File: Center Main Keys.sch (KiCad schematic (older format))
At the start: 9 parts

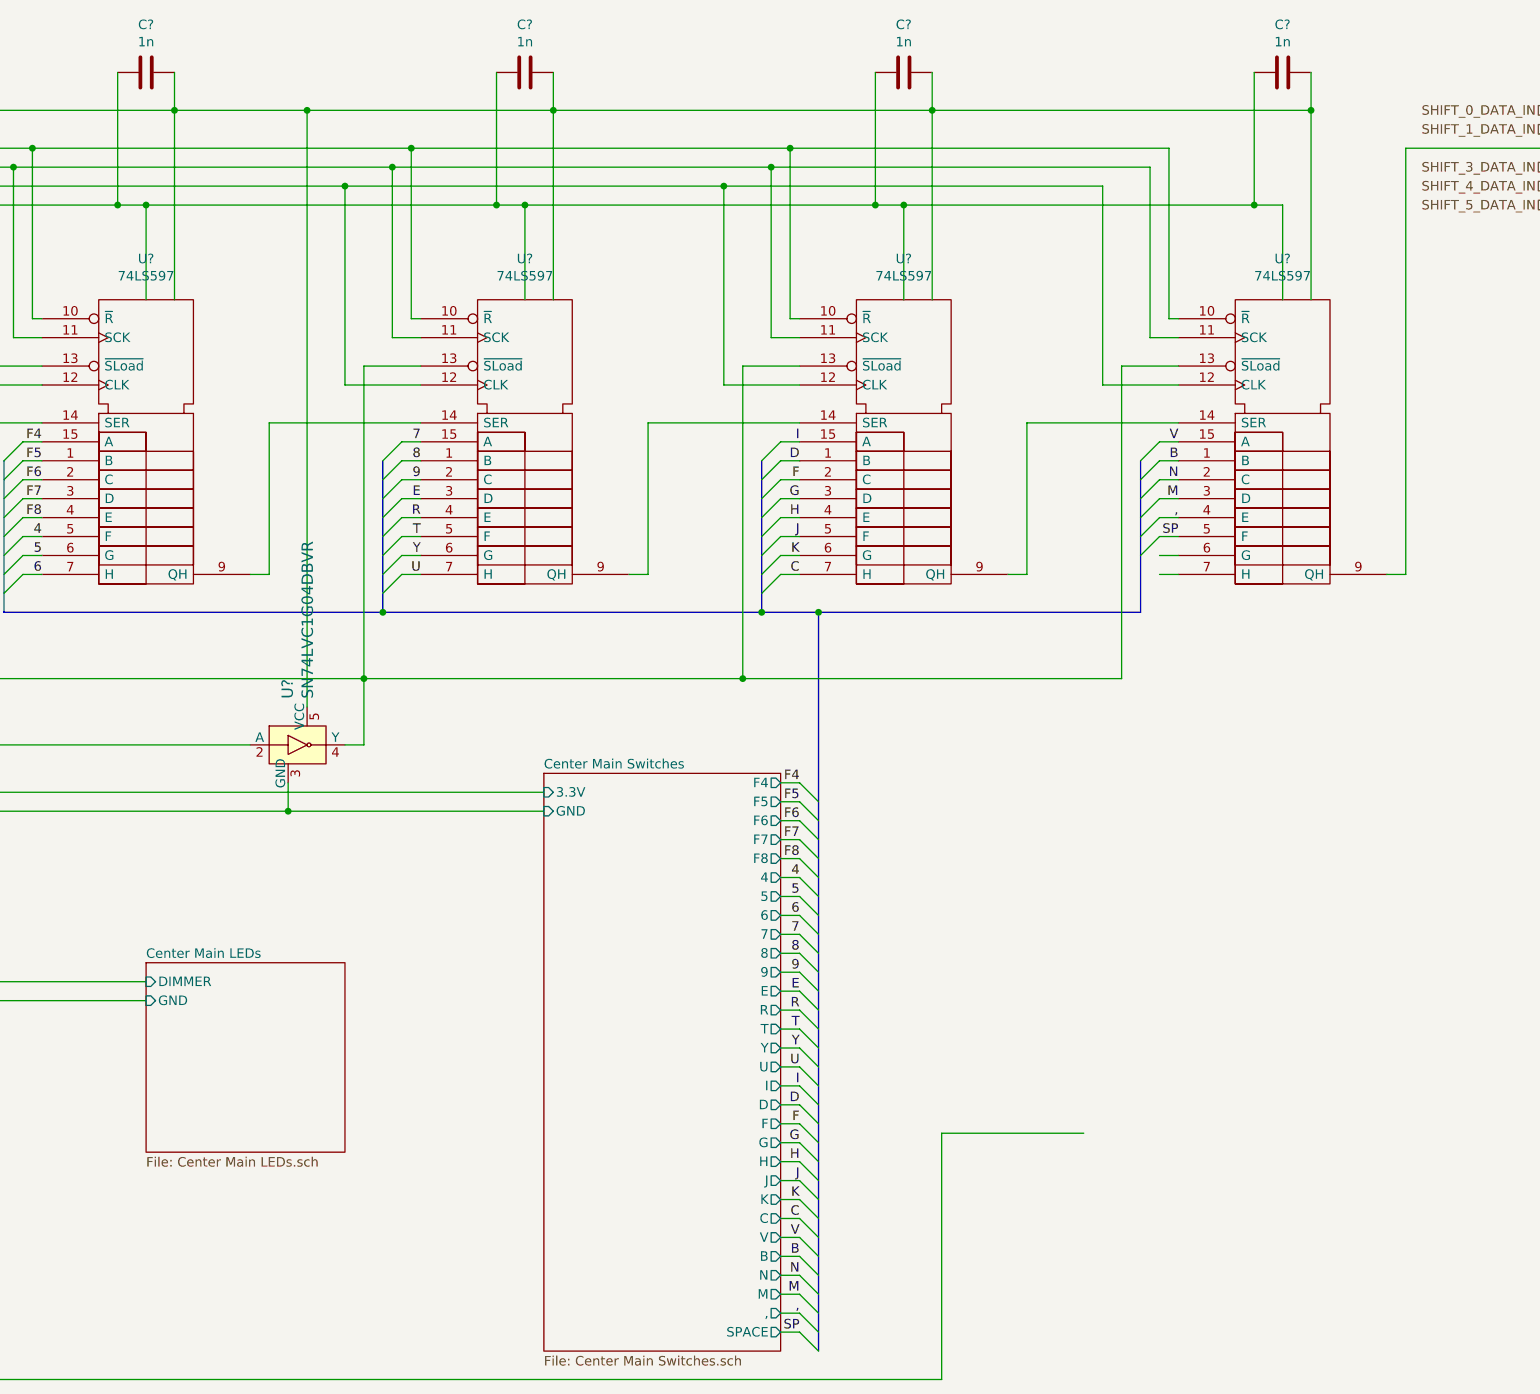
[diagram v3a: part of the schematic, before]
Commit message: Corrected errors found in design rule check
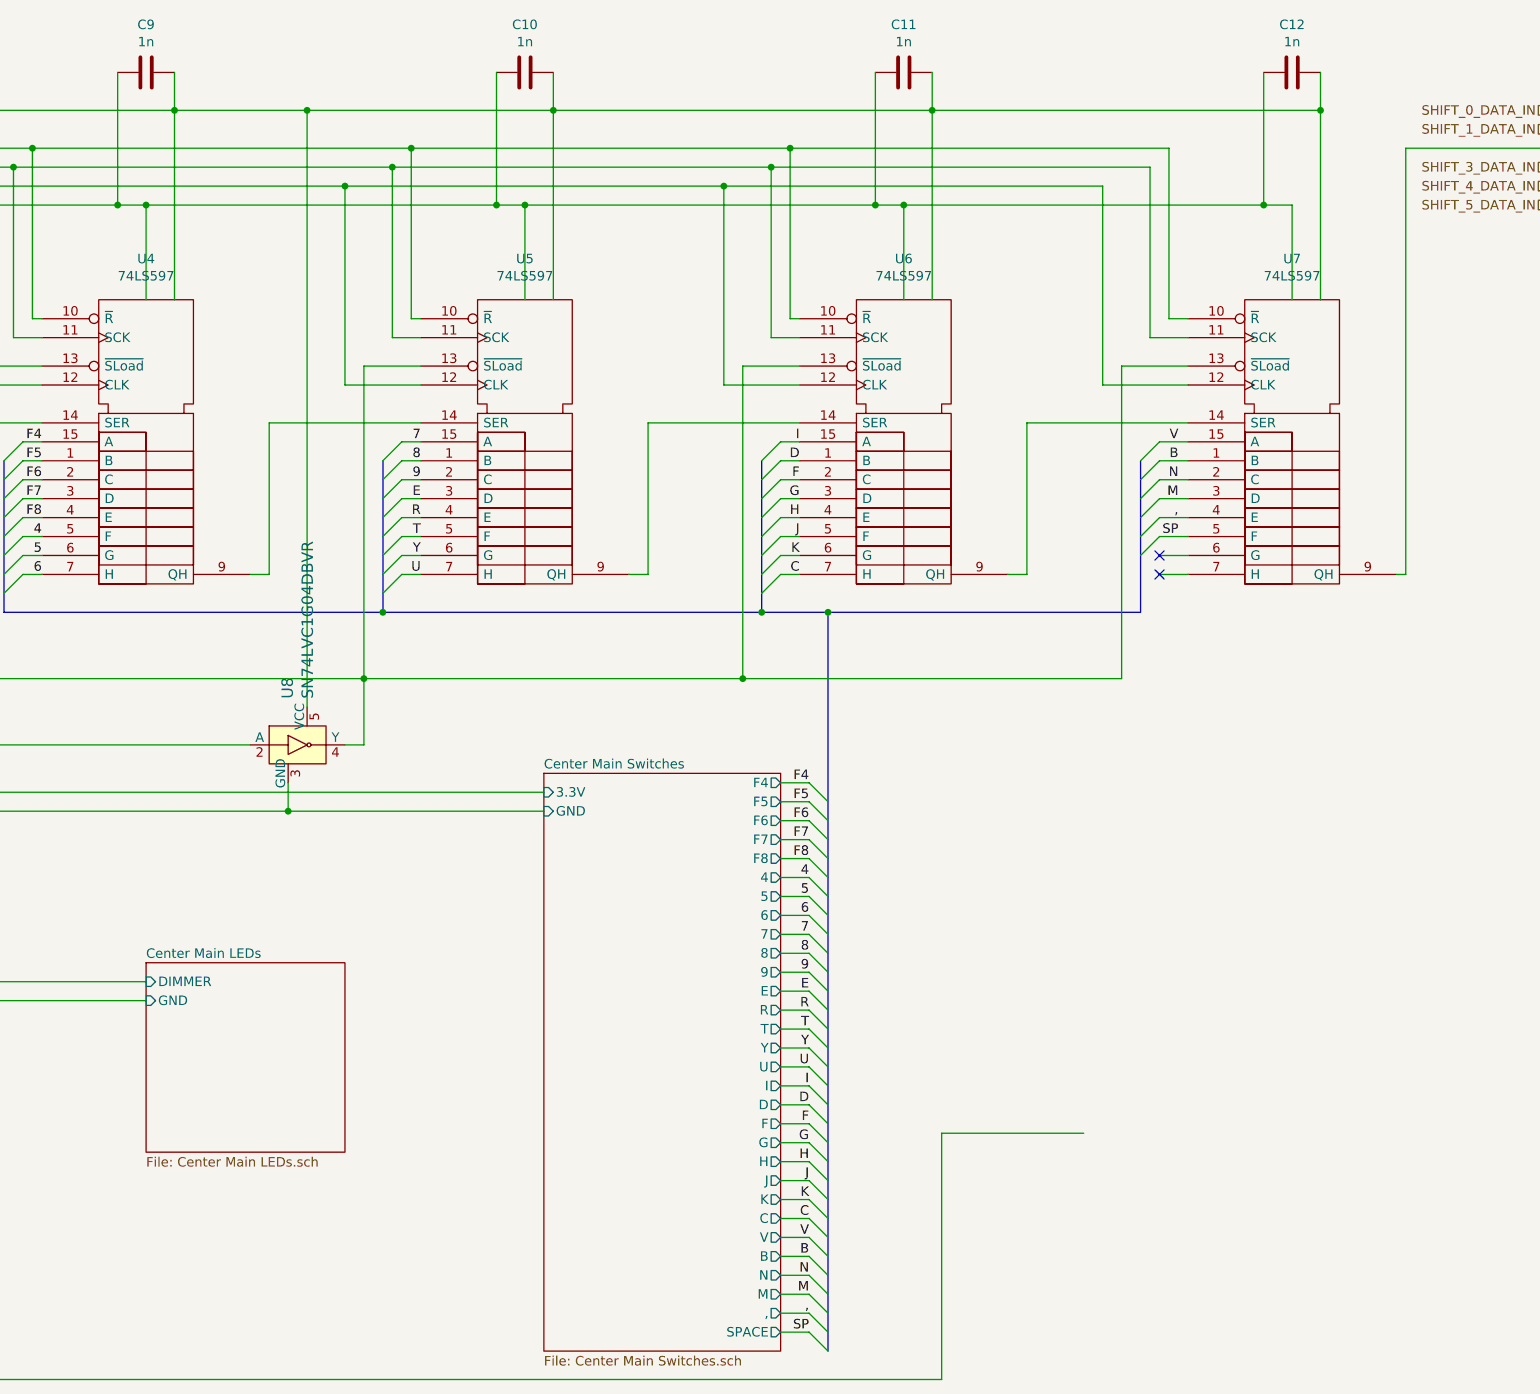
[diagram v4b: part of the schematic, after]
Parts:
- C10, C11, C12, C9: renamed from C?; footprint (none) -> Capacitor_SMD:C_1206_3216Metric_Pad1.42x1.75mm_HandSolder
- U4, U5, U6, U7: renamed from U?; footprint (none) -> Package_SO:SOIC-16_3.9x9.9mm_P1.27mm
- gave numbers to parts that had none: 1
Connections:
- no-connect marks 0 -> 2
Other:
- moved on the sheet: C12, U7

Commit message: Redesigned for single large PCB
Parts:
- added C13, C14, C15, C16, C17, C18, C19, C20, C21, C22: 1n, Capacitor_SMD:C_1206_3216Metric_Pad1.42x1.75mm_HandSolder, symbol Device:C
- added U10, U11, U12, U13, U14, U15, U16, U17, U18, U9: 74LS597, Package_SO:SOIC-16_3.9x9.9mm_P1.27mm, symbol 74xx_IEEE:74LS597
- renumbered U8 to U4, U4 to U5, U5 to U6, U6 to U7, U7 to U8
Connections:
- net ,: now also U13.5 (F); no longer U8.4 (E)
- net 4: now also U10.6 (G); no longer U5.5 (F)
- net 5: now also U10.7 (H); no longer U5.6 (G)
- net 6: now also U11.15 (A); no longer U5.7 (H)
- net 7: now also U11.1 (B); no longer U6.15 (A)
- net 8: now also U11.2 (C); no longer U6.1 (B)
- net 9: now also U11.3 (D); no longer U6.2 (C)
- net B: now also U13.2 (C); no longer U8.1 (B)
- net C: now also U13.15 (A); no longer U7.7 (H)
- net D: now also U12.2 (C); no longer U7.1 (B)
- net E: now also U11.4 (E); no longer U6.3 (D)
- net F: now also U12.3 (D); no longer U7.2 (C)
- net F4: now also U10.1 (B); no longer U5.15 (A)
- net F5: now also U10.2 (C); no longer U5.1 (B)
- net F6: now also U10.3 (D); no longer U5.2 (C)
- net F7: now also U10.4 (E); no longer U5.3 (D)
- net F8: now also U10.5 (F); no longer U5.4 (E)
- net G: now also U12.4 (E); no longer U7.3 (D)
- net GND: now also C13.2, C14.2, C15.2, C16.2, C17.2, C18.2, C19.2, C20.2, C21.2, C22.2, U10.8 (GND), U11.8 (GND), U12.8 (GND), U13.8 (GND), U14.8 (GND), U15.8 (GND), U16.8 (GND), U17.8 (GND), U18.8 (GND), U9.8 (GND)
- net H: now also U12.5 (F); no longer U7.4 (E)
- net I: now also U12.1 (B); no longer U7.15 (A)
- net J: now also U12.6 (G); no longer U7.5 (F)
- net K: now also U12.7 (H); no longer U7.6 (G)
- net M: now also U13.4 (E); no longer U8.3 (D)
- net N: now also U13.3 (D); no longer U8.2 (C)
- net R: now also U11.5 (F); no longer U6.4 (E)
- net RESET: now also U10.10 (~R), U11.10 (~R), U12.10 (~R), U13.10 (~R), U14.10 (~R), U15.10 (~R), U16.10 (~R), U17.10 (~R), U18.10 (~R), U9.10 (~R)
- net SHIFT_CLK: now also U10.11 (SCK), U11.11 (SCK), U12.11 (SCK), U13.11 (SCK), U14.11 (SCK), U15.11 (SCK), U16.11 (SCK), U17.11 (SCK), U18.11 (SCK), U9.11 (SCK)
- net SHIFT_RCLK: now also U10.12 (CLK), U11.12 (CLK), U12.12 (CLK), U13.12 (CLK), U14.12 (CLK), U15.12 (CLK), U16.12 (CLK), U17.12 (CLK), U18.12 (CLK), U9.12 (CLK)
- net SP: now also U13.6 (G); no longer U8.5 (F)
- net T: now also U11.6 (G); no longer U6.5 (F)
- net U: now also U12.15 (A); no longer U6.7 (H)
- net V: now also U13.1 (B); no longer U8.15 (A)
- net VCC: now also C13.1, C14.1, C15.1, C16.1, C17.1, C18.1, C19.1, C20.1, C21.1, C22.1, U10.16 (VCC), U11.16 (VCC), U12.16 (VCC), U13.16 (VCC), U14.16 (VCC), U15.16 (VCC), U16.16 (VCC), U17.16 (VCC), U18.16 (VCC), U9.16 (VCC)
- net Y: now also U11.7 (H); no longer U6.6 (G)
- net at U4.4 (Y), U5.13 (~SLoad), U6.13 (~SLoad)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: now also U10.13 (~SLoad), U11.13 (~SLoad), U12.13 (~SLoad), U13.13 (~SLoad), U14.13 (~SLoad), U15.13 (~SLoad), U16.13 (~SLoad), U17.13 (~SLoad), U18.13 (~SLoad), U9.13 (~SLoad)
- net Q: now reaches U8.6 (G)
- net W: now reaches U8.7 (H)
- net SHIFT_2_DATA: no longer names the net of U8.9 (QH)
- net SHIFT_2_DATA: now also U9.14 (SER)
- new net: U10.14 (SER), U9.9 (QH)
- new net: U10.9 (QH), U11.14 (SER)
- new net: U11.9 (QH), U12.14 (SER)
- new net: U12.9 (QH), U13.14 (SER)
- new net: U13.9 (QH), U14.14 (SER)
- new net: U14.9 (QH), U15.14 (SER)
- new net: U15.9 (QH), U16.14 (SER)
- new net: U16.9 (QH), U17.14 (SER)
- new net: U17.9 (QH), U18.14 (SER)
- new net ': U15.6 (G)
- new net -: U14.4 (E)
- new net .: U16.15 (A)
- new net 0: U14.3 (D)
- new net 1: U8.2 (C)
- new net 2: U8.3 (D)
- new net 3: U8.4 (E)
- new net ;: U15.5 (F)
- new net =: U14.5 (F)
- new net A: U9.1 (B)
- new net APP: U16.5 (F)
- new net BACK: U14.6 (G)
- new net CAPL: U9.15 (A)
- new net DEL: U17.5 (F)
- new net DN: U18.2 (C)
- new net END: U17.6 (G)
- new net ENTER: U15.7 (H)
- new net ESC: U7.5 (F)
- new net EXT1: U7.1 (B)
- new net EXT10: U18.6 (G)
- new net EXT2: U7.2 (C)
- new net EXT3: U7.3 (D)
- new net EXT4: U7.4 (E)
- new net EXT8: U18.4 (E)
- new net EXT9: U18.5 (F)
- new net F1: U7.6 (G)
- new net F10: U14.15 (A)
- new net F11: U14.1 (B)
- new net F12: U14.2 (C)
- new net F2: U7.7 (H)
- new net F3: U8.15 (A)
- new net F9: U13.7 (H)
- new net HOME: U17.3 (D)
- new net INS: U17.2 (C)
- new net L: U15.4 (E)
- new net LALT: U10.15 (A)
- new net LCTRL: U9.6 (G)
- new net LSHFT: U9.3 (D)
- new net LT: U18.1 (B)
- new net LWIND: U9.7 (H)
- new net NUM*: U5.2 (C)
- new net NUM+: U5.7 (H)
- new net NUM-: U5.3 (D)
- new net NUM.: U7.15 (A)
- new net NUM0: U6.7 (H)
- new net NUM1: U6.3 (D)
- new net NUM2: U6.4 (E)
- new net NUM3: U6.5 (F)
- new net NUM4: U6.15 (A)
- new net NUM5: U6.1 (B)
- new net NUM6: U6.2 (C)
- new net NUM7: U5.4 (E)
- new net NUM8: U5.5 (F)
- new net NUM9: U5.6 (G)
- new net NUME: U6.6 (G)
- new net NUML: U5.15 (A)
- new net NUMS: U5.1 (B)
- new net O: U14.7 (H)
- new net P: U15.15 (A)
- new net PAUS: U17.1 (B)
- new net PGDN: U17.7 (H)
- new net PGUP: U17.4 (E)
- new net PRNT: U16.7 (H)
- new net RALT: U16.3 (D)
- new net RCTRL: U16.6 (G)
- new net RSHFT: U16.2 (C)
- new net RT: U18.3 (D)
- new net RWIND: U16.4 (E)
- new net S: U9.2 (C)
- new net SCRL: U17.15 (A)
- new net SHIFT_DATA: U18.9 (QH)
- new net SLSH: U16.1 (B)
- new net TAB: U8.5 (F)
- new net UP: U18.15 (A)
- new net X: U9.5 (F)
- new net Z: U9.4 (E)
- new net [: U15.1 (B)
- new net \: U15.3 (D)
- new net ]: U15.2 (C)
- new net `: U8.1 (B)
- no-connect marks 2 -> 1
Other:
- moved on the sheet: C10, C11, C12, C9, U4, U5, U6, U7, U8

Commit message: PCB Routed, minor circuit changes
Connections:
- net ': now also U15.2 (C); no longer U15.6 (G)
- net ,: now also U13.3 (D); no longer U13.5 (F)
- net -: now also U14.5 (F); no longer U14.4 (E)
- net .: now also U14.1 (B); no longer U16.15 (A)
- net 1: now also U8.3 (D); no longer U8.2 (C)
- net 2: now also U9.3 (D); no longer U8.3 (D)
- net 3: now also U10.15 (A); no longer U8.4 (E)
- net 4: now also U10.5 (F); no longer U10.6 (G)
- net 5: now also U11.4 (E); no longer U10.7 (H)
- net 6: now also U11.6 (G); no longer U11.15 (A)
- net 7: now also U12.3 (D); no longer U11.1 (B)
- net 8: now also U13.15 (A); no longer U11.2 (C)
- net 9: now also U13.5 (F); no longer U11.3 (D)
- net ;: now also U14.7 (H); no longer U15.5 (F)
- net =: now also U15.5 (F); no longer U14.5 (F)
- net A: now also U8.5 (F); no longer U9.1 (B)
- net APP: now also U15.7 (H); no longer U16.5 (F)
- net B: now also U11.1 (B); no longer U13.2 (C)
- net BACK: now also U16.4 (E); no longer U14.6 (G)
- net C: now also U10.2 (C); no longer U13.15 (A)
- net CAPL: now also U7.7 (H); no longer U9.15 (A)
- net D: now also U9.6 (G); no longer U12.2 (C)
- net DEL: now also U17.2 (C); no longer U17.5 (F)
- net DN: now also U18.1 (B); no longer U18.2 (C)
- net E: now also U9.7 (H); no longer U11.4 (E)
- net ENTER: now also U16.1 (B); no longer U15.7 (H)
- net ESC: now also U8.2 (C); no longer U7.5 (F)
- net EXT1: now also U5.5 (F); no longer U7.1 (B)
- net EXT2: now also U6.2 (C); no longer U7.2 (C)
- net EXT3: now also U7.15 (A); no longer U7.3 (D)
- net EXT8: now also U17.3 (D); no longer U18.4 (E)
- net EXT9: now also U17.7 (H); no longer U18.5 (F)
- net F: now also U10.3 (D); no longer U12.3 (D)
- net F1: now also U9.4 (E); no longer U7.6 (G)
- net F10: now also U15.4 (E); no longer U14.15 (A)
- net F11: now also U15.6 (G); no longer U14.1 (B)
- net F12: now also U16.5 (F); no longer U14.2 (C)
- net F2: now also U10.1 (B); no longer U7.7 (H)
- net F3: now also U10.6 (G); no longer U8.15 (A)
- net F4: now also U11.5 (F); no longer U10.1 (B)
- net F5: now also U12.2 (C); no longer U10.2 (C)
- net F6: now also U12.7 (H); no longer U10.3 (D)
- net F7: now also U13.4 (E); no longer U10.4 (E)
- net F8: now also U14.2 (C); no longer U10.5 (F)
- net F9: now also U14.4 (E); no longer U13.7 (H)
- net G: now also U11.2 (C); no longer U12.4 (E)
- net H: now also U12.15 (A); no longer U12.5 (F)
- net HOME: now also U17.5 (F); no longer U17.3 (D)
- net I: now also U13.1 (B); no longer U12.1 (B)
- net INS: now also U17.1 (B); no longer U17.2 (C)
- net J: now also U12.5 (F); no longer U12.6 (G)
- net K: now also U13.2 (C); no longer U12.7 (H)
- net L: now also U13.7 (H); no longer U15.4 (E)
- net LALT: now also U9.15 (A); no longer U10.15 (A)
- net LCTRL: now also U7.5 (F); no longer U9.6 (G)
- net LSHFT: now also U7.6 (G); no longer U9.3 (D)
- net LT: now also U18.15 (A); no longer U18.1 (B)
- net LWIND: now also U8.7 (H); no longer U9.7 (H)
- net M: now also U12.6 (G); no longer U13.4 (E)
- net N: now also U12.1 (B); no longer U13.3 (D)
- net NUM*: now also U6.7 (H); no longer U5.2 (C)
- net NUM+: now also U7.2 (C); no longer U5.7 (H)
- net NUM-: now also U7.3 (D); no longer U5.3 (D)
- net NUM.: now also U6.3 (D); no longer U7.15 (A)
- net NUM0: now also U5.15 (A); no longer U6.7 (H)
- net NUM1: now also U5.1 (B); no longer U6.3 (D)
- net NUM2: now also U5.6 (G); no longer U6.4 (E)
- net NUM3: now also U6.4 (E); no longer U6.5 (F)
- net NUM4: now also U5.2 (C); no longer U6.15 (A)
- net NUM5: now also U5.7 (H); no longer U6.1 (B)
- net NUM6: now also U6.5 (F); no longer U6.2 (C)
- net NUM7: now also U5.3 (D); no longer U5.4 (E)
- net NUM8: now also U6.15 (A); no longer U5.5 (F)
- net NUM9: now also U6.6 (G); no longer U5.6 (G)
- net NUME: now also U7.1 (B); no longer U6.6 (G)
- net NUML: now also U5.4 (E); no longer U5.15 (A)
- net NUMS: now also U6.1 (B); no longer U5.1 (B)
- net O: now also U13.6 (G); no longer U14.7 (H)
- net P: now also U14.6 (G); no longer U15.15 (A)
- net PAUS: now also U18.3 (D); no longer U17.1 (B)
- net PGDN: now also U18.5 (F); no longer U17.7 (H)
- net PGUP: now also U18.4 (E); no longer U17.4 (E)
- net PRNT: now also U17.15 (A); no longer U16.7 (H)
- net Q: now also U8.4 (E); no longer U8.6 (G)
- net R: now also U10.4 (E); no longer U11.5 (F)
- net RALT: now also U14.15 (A); no longer U16.3 (D)
- net RSHFT: now also U16.15 (A); no longer U16.2 (C)
- net RT: now also U18.7 (H); no longer U18.3 (D)
- net RWIND: now also U15.15 (A); no longer U16.4 (E)
- net S: now also U9.1 (B); no longer U9.2 (C)
- net SCRL: now also U17.4 (E); no longer U17.15 (A)
- net SLSH: now also U15.1 (B); no longer U16.1 (B)
- net SP: now also U11.15 (A); no longer U13.6 (G)
- net T: now also U11.3 (D); no longer U11.6 (G)
- net TAB: now also U8.15 (A); no longer U8.5 (F)
- net U: now also U12.4 (E); no longer U12.15 (A)
- net UP: now also U18.2 (C); no longer U18.15 (A)
- net V: now also U10.7 (H); no longer U13.1 (B)
- net W: now also U9.2 (C); no longer U8.7 (H)
- net Z: now also U8.6 (G); no longer U9.4 (E)
- net [: now also U15.3 (D); no longer U15.1 (B)
- net \: now also U16.3 (D); no longer U15.3 (D)
- net ]: now also U16.2 (C); no longer U15.2 (C)
